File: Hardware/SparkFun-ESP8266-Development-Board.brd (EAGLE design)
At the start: 55.3 x 25.9 mm, 67 parts, among them J1 U.FL, Q1 2.5A/30V, Q2 MMBT2222A, U1 ESP8266, U2 MCP73831, U3 AT25SF041-SOIC8, U4 AP2112K-3.3V, U5 ATECC108-SSHDA, Y1 26MHz

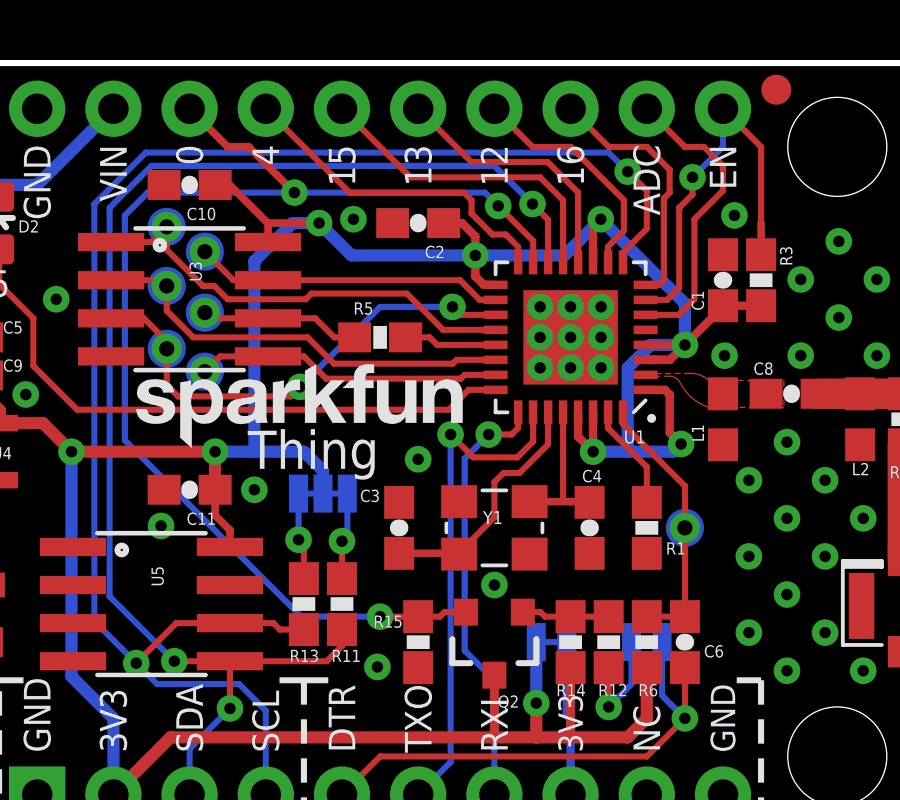
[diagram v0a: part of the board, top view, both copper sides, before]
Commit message: Straightening out some nets coming out of ESP8266. Value JP5. Flag label on RESET.
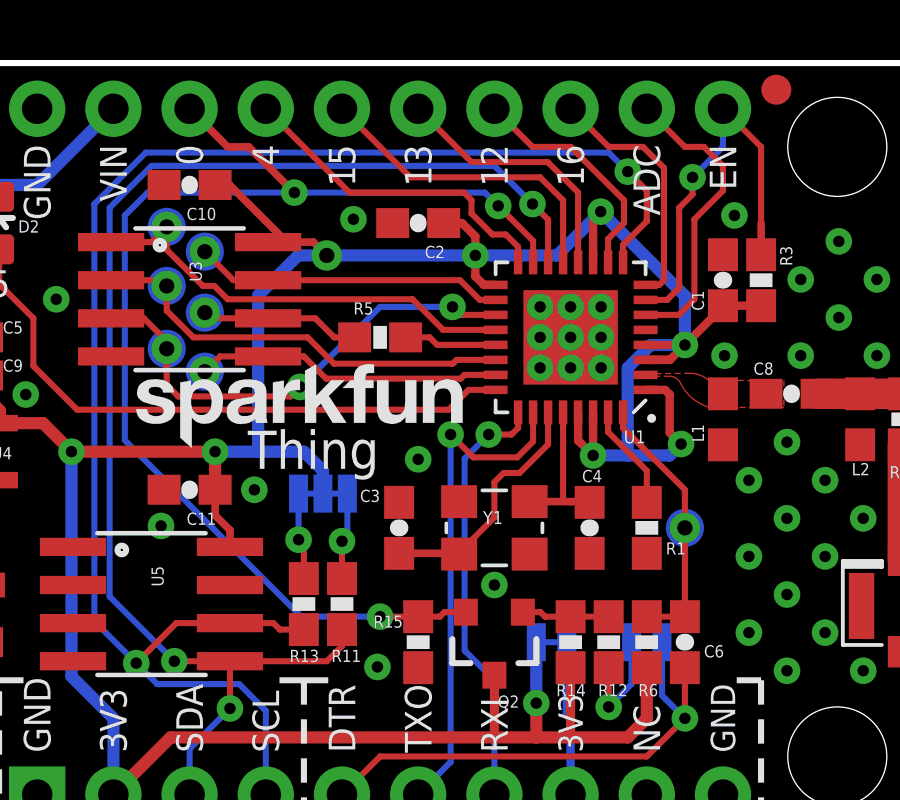
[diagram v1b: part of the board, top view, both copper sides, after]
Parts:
- JP5: value (none) -> I2C

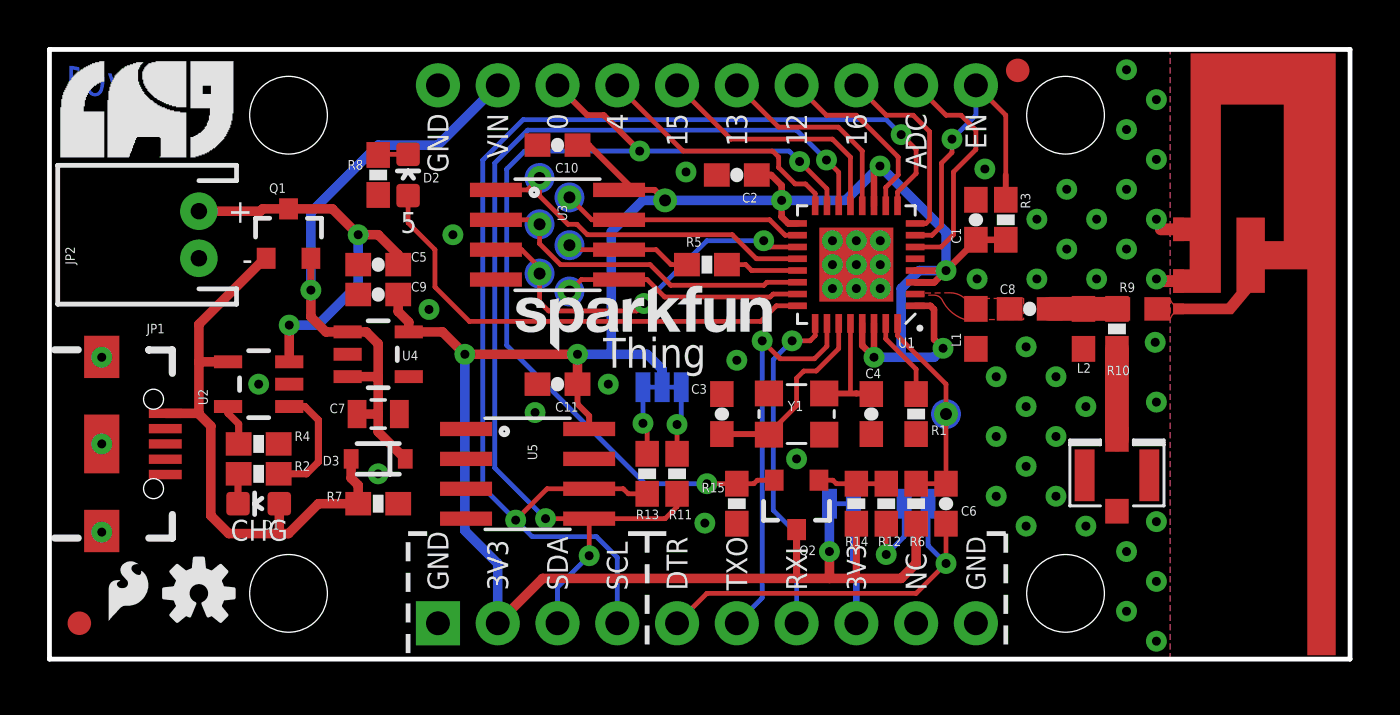
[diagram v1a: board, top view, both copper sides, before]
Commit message: Adding power LED. Re-arranging power circuitry. Breaking out pin 5.
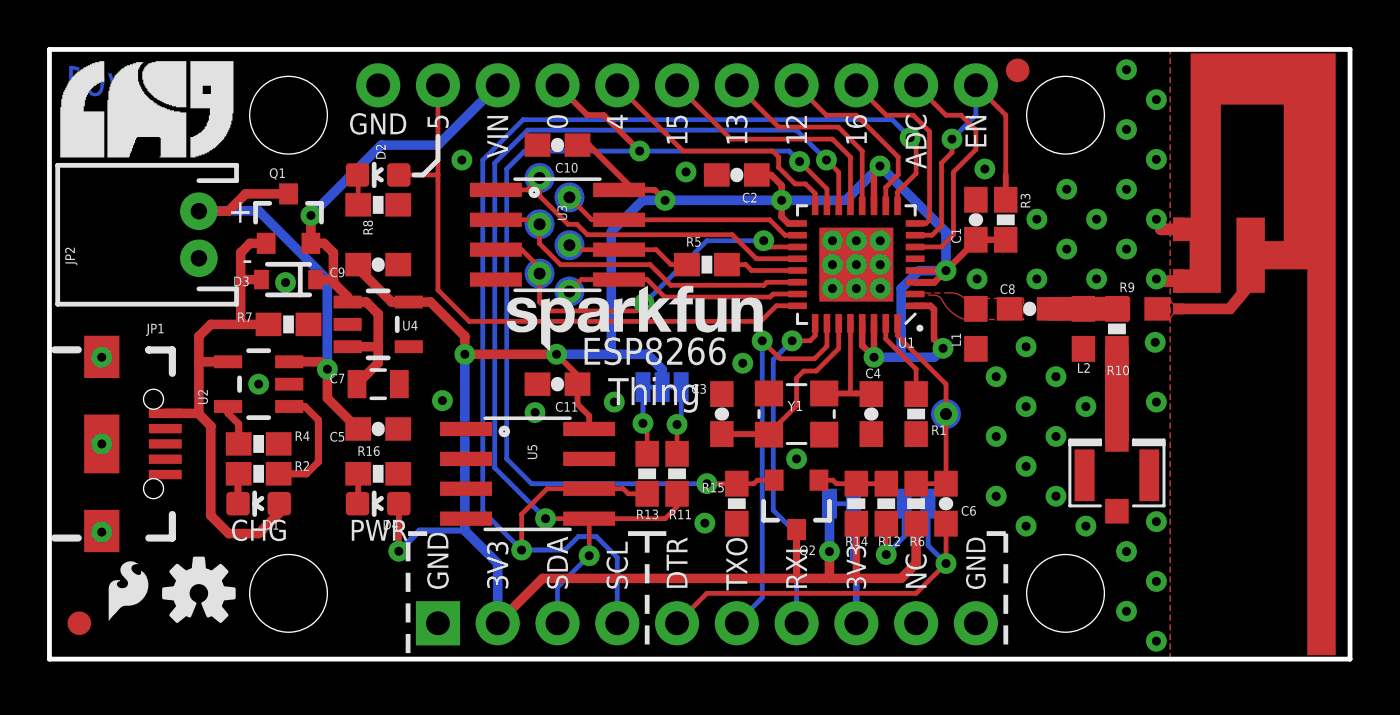
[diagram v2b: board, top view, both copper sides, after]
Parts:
- removed JP3: M10SILK_FEMALE_PTH, SparkFun-Connectors:1X10
- added D4: GREEN, SparkFun-LED:LED-0603
- added JP6: M11PTH, SparkFun-Connectors:1X11
- added R16: 200, SparkFun-Resistors:0603-RES
- moved D3 8.52 mm to (10.2, 16.1)
- moved R7 8.52 mm to (10.2, 14.2)
- moved C5 6.98 mm to (14.0, 9.78), turned to 0 degrees
- moved R8 1.27 mm to (14.0, 19.3), turned to 0 degrees
- moved C7 1.27 mm to (14.0, 11.7)
- moved C9 1.27 mm to (14.0, 16.8), turned to 0 degrees
- moved D2 1.27 mm to (14.0, 20.6), turned to 90 degrees
- moved U4 1.27 mm to (14.0, 14.2)
- moved Q1 0.64 mm to (10.2, 18.7)
- moved LOGO2 0.38 mm to (18.9, 12.6)
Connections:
- new net N$4: D4.C, R16.1
- net ADC: now also JP6.10; no longer JP3.9
- net CHIP_EN: now also JP6.11; no longer JP3.10
- net GND: now also JP6.1, R16.2; no longer JP3.1
- net GPIO0: now also JP6.4; no longer JP3.3
- net GPIO12: now also JP6.8; no longer JP3.7
- net GPIO13: now also JP6.7; no longer JP3.6
- net GPIO15: now also JP6.6; no longer JP3.5
- net GPIO16: now also JP6.9; no longer JP3.8
- net GPIO4: now also JP6.5; no longer JP3.4
- net GPIO5: now also JP6.2
- net VCC: now also D4.A
- net VIN: now also JP6.3; no longer JP3.2
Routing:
- net VCC: track 112.0 -> 119.7 mm, vias 9 -> 10
- net GPIO5: track 20.6 -> 26.5 mm
- net VIN: track 26.9 -> 21.8 mm
- net GPIO0: track 41.3 -> 44.1 mm
- net VUSB: track 25.5 -> 22.8 mm
- net GPIO14/SCL: track 52.2 -> 54.6 mm
- net VBAT: track 17.1 -> 19.4 mm, vias 2 -> 1
- net N$4: track 0.00 -> 1.28 mm
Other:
- board text added: "ESP8266 Thing"
- board text added: "PWR"
- board text removed: "Thing"

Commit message: Fixing net names for flash signals. Updating bottom silk labels
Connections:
- net SD_CMD renamed SD_CS0
- net SD_D0 renamed SD_SO
- net SD_D1 renamed SD_SI
- net SD_D2 renamed SD_!HD!
- net SD_D3 renamed SD_!WP!
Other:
- board text added: "!CS!"
- board text added: "!HD!"
- board text added: "!WP!"
- board text added: "SI"
- board text added: "SO"
- board text removed: "CMD"
- board text removed: "D0"
- board text removed: "D1"
- board text removed: "D2"
- board text removed: "D3"
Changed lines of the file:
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@@
 <rectangle x1="4.50900625" y1="25.367615625" x2="5.81710625" y2="25.411046875" layer="21"/>
 <rectangle x1="5.989828125" y1="25.367615625" x2="7.821165625" y2="25.411046875" layer="21"/>
-<text x="20.0025" y="20.447" size="0.8636" layer="22" font="vector" ratio="15" rot="MR0" align="center-left">CMD</text>
-<text x="20.0025" y="18.4785" size="0.8636" layer="22" font="vector" ratio="15" rot="MR0" align="center-left">D0</text>
-<text x="20.0025" y="16.383" size="0.8636" layer="22" font="vector" ratio="15" rot="MR0" align="center-left">D3</text>
-<text x="22.733" y="19.6215" size="0.8636" layer="22" font="vector" ratio="15" rot="MR0" align="center-right">D2</text>
+<text x="20.0025" y="20.447" size="0.8636" layer="22" font="vector" ratio="15" rot="MR0" align="center-left">!CS!</text>
+<text x="20.0025" y="18.4785" size="0.8636" layer="22" font="vector" ratio="15" rot="MR0" align="center-left">SO</text>
+<text x="20.0025" y="16.383" size="0.8636" layer="22" font="vector" ratio="15" rot="MR0" align="center-left">!WP!</text>
+<text x="22.733" y="19.6215" size="0.8636" layer="22" font="vector" ratio="15" rot="MR0" align="center-right">!HD!</text>
 <text x="22.733" y="17.5895" size="0.8636" layer="22" font="vector" ratio="15" rot="MR0" align="center-right">CLK</text>
-<text x="22.733" y="15.621" size="0.8636" layer="22" font="vector" ratio="15" rot="MR0" align="center-right">D1</text>
+<text x="22.733" y="15.621" size="0.8636" layer="22" font="vector" ratio="15" rot="MR0" align="center-right">SI</text>
 <dimension x1="0" y1="0" x2="0" y2="25.908" x3="-7.874" y3="12.954" textsize="0.8636" textratio="15" layer="49" unit="inch"/>
 <dimension x1="0" y1="0" x2="55.2704" y2="0" x3="27.6352" y3="-6.096" textsize="0.8636" textratio="15" layer="49" unit="inch"/>
@@
 <text x="8.636" y="17.018" size="1.016" layer="21" font="vector" ratio="15" align="center-right">-</text>
 <text x="13.97" y="23.0632" size="0.889" layer="22" font="vector" ratio="15" rot="MR90" align="center-right">GND</text>
-<text x="19.05" y="23.0632" size="0.889" layer="22" font="vector" ratio="15" rot="MR90" align="center-right">VIN</text>
+<text x="19.05" y="22.9362" size="0.889" layer="22" font="vector" ratio="15" rot="MR0" align="top-center">VIN</text>
 <text x="21.59" y="23.0632" size="0.889" layer="22" font="vector" ratio="15" rot="MR90" align="center-right">0</text>
 <text x="24.13" y="23.0632" size="0.889" layer="22" font="vector" ratio="15" rot="MR90" align="center-right">4</text>
@@
 <contactref element="JP6" pad="5"/>
 </signal>
-<signal name="SD_D3">
+<signal name="SD_!WP!">
 <contactref element="U1" pad="19"/>
 <contactref element="U3" pad="3"/>
@@
 <contactref element="TP1" pad="P$1"/>
 </signal>
-<signal name="SD_D2">
+<signal name="SD_!HD!">
 <contactref element="U1" pad="18"/>
 <contactref element="U3" pad="7"/>
@@
 <contactref element="TP4" pad="P$1"/>
 </signal>
-<signal name="SD_D1">
+<signal name="SD_SI">
 <contactref element="U1" pad="23"/>
 <contactref element="U3" pad="5"/>
@@
 <contactref element="TP2" pad="P$1"/>
 </signal>
-<signal name="SD_D0">
+<signal name="SD_SO">
 <contactref element="U1" pad="22"/>
 <contactref element="U3" pad="2"/>
@@
 <contactref element="TP3" pad="P$1"/>
 </signal>
-<signal name="SD_CMD">
+<signal name="SD_CS0">
 <contactref element="U1" pad="20"/>
 <contactref element="U3" pad="1"/>

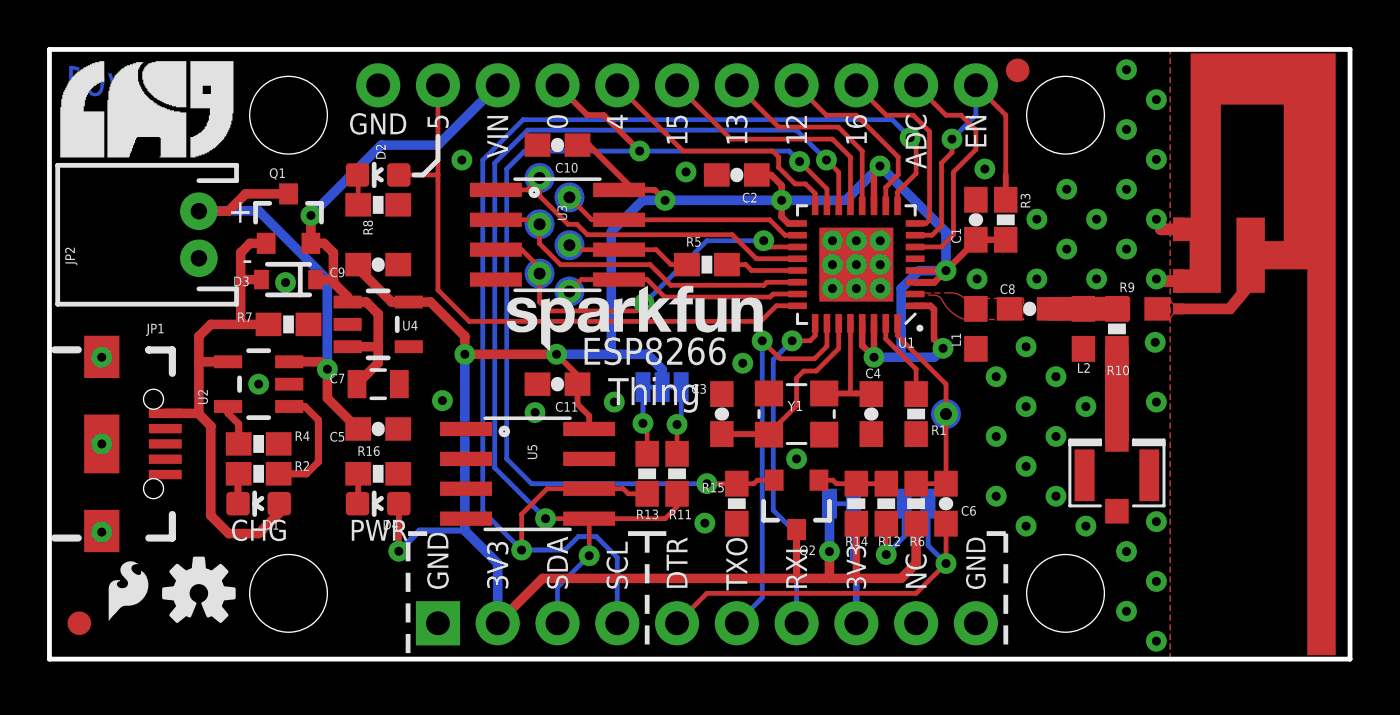
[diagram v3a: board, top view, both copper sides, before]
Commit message: Adding pull-down resistor to GPIO15 (required to upload). Not broken out any more.
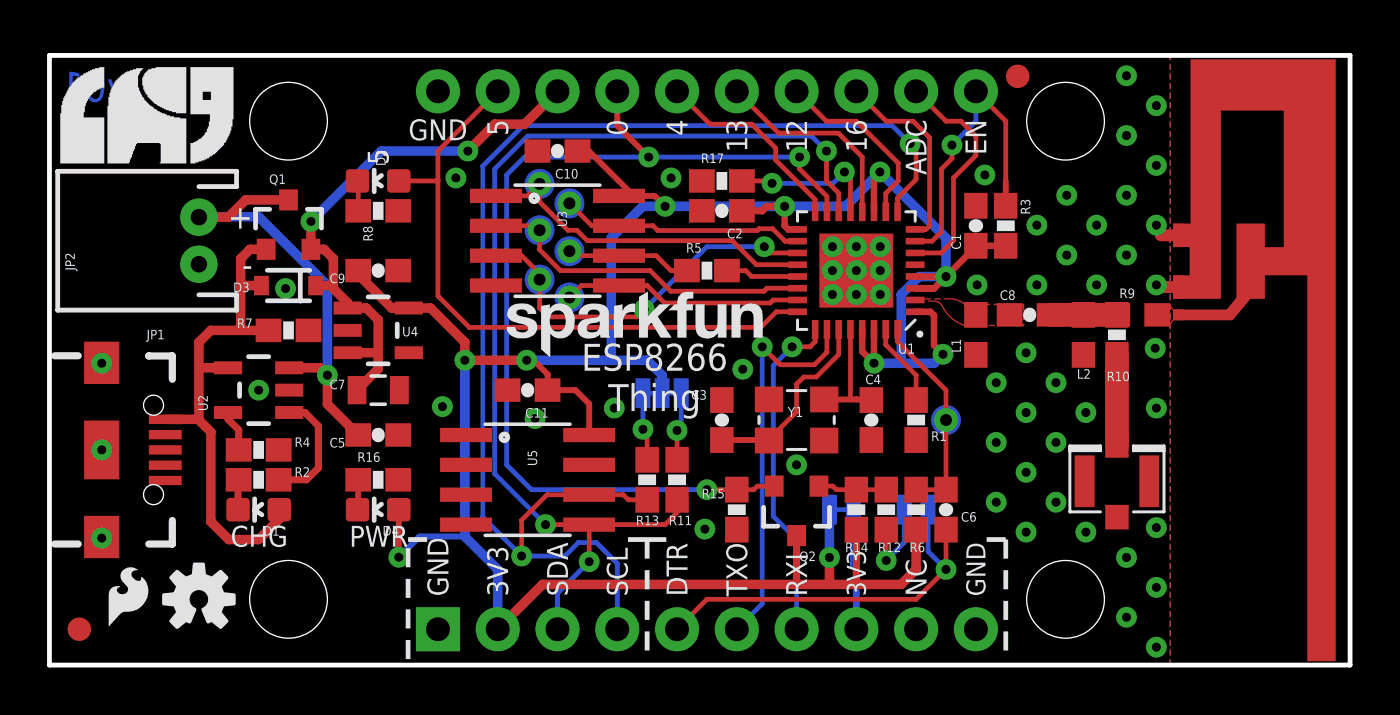
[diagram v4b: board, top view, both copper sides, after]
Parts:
- removed JP6: M11PTH, SparkFun-Connectors:1X11
- added JP3: M10", SparkFun-Connectors:1X10
- added R17: 10K, SparkFun-Resistors:0603-RES
- moved C2 1.65 mm to (28.6, 19.1)
- moved C11 1.30 mm to (20.3, 11.4)
- moved C1 0.25 mm to (39.4, 18.4)
- moved C10 0.25 mm to (21.6, 21.6)
- moved D2 0.25 mm to (14.0, 20.3)
- moved D3 0.25 mm to (10.2, 15.9)
- moved LOGO1 0.25 mm to (23.0, 11.7)
- moved Q1 0.25 mm to (10.2, 18.4)
- moved R3 0.25 mm to (40.6, 18.4)
- moved STANDOFF1 0.25 mm to (43.2, 22.9)
- moved STANDOFF3 0.25 mm to (10.2, 22.9)
- moved TP3 0.25 mm to (22.1, 17.3)
- moved TP4 0.25 mm to (22.1, 19.4)
- moved TP5 0.25 mm to (20.8, 18.2)
- moved C6 0.25 mm to (38.1, 6.35)
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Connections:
- net ADC: now also JP3.9; no longer JP6.10
- net CHIP_EN: now also JP3.10; no longer JP6.11
- net GND: now also JP3.1, R17.1; no longer JP6.1
- net GPIO0: now also JP3.4; no longer JP6.4
- net GPIO12: now also JP3.7; no longer JP6.8
- net GPIO13: now also JP3.6; no longer JP6.7
- net GPIO15: now also R17.2; no longer JP6.6
- net GPIO16: now also JP3.8; no longer JP6.9
- net GPIO4: now also JP3.5; no longer JP6.5
- net GPIO5: now also JP3.2; no longer JP6.2
- net VIN: now also JP3.3; no longer JP6.3
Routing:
- net GPIO15: track 10.7 -> 6.40 mm, vias 0 -> 2
- net VIN: track 21.8 -> 24.3 mm, vias 1 -> 2
- net GPIO4: track 11.1 -> 8.59 mm
- net VCC: track 119.7 -> 121.1 mm
- net GPIO5: track 26.5 -> 27.5 mm
- net GPIO0: track 44.1 -> 43.1 mm
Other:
- board text removed: "15"
